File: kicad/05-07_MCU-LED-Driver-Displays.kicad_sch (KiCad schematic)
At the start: 57 parts, among them J4 Conn_01x03_Pin, J5 Conn_01x03_Pin, J7 Conn_02x05_Counter_Clockwise, Q4 AO3400A, Q5 AO3400A, SW1 USER_A, SW2 USER_B_PWR, SW3 RESET, SW4 BOOTSEL, U5 W25Q128JVS, U6 RP2040, Y1 ABM8-272-T3, Y2 ABS06-32.768-9-T

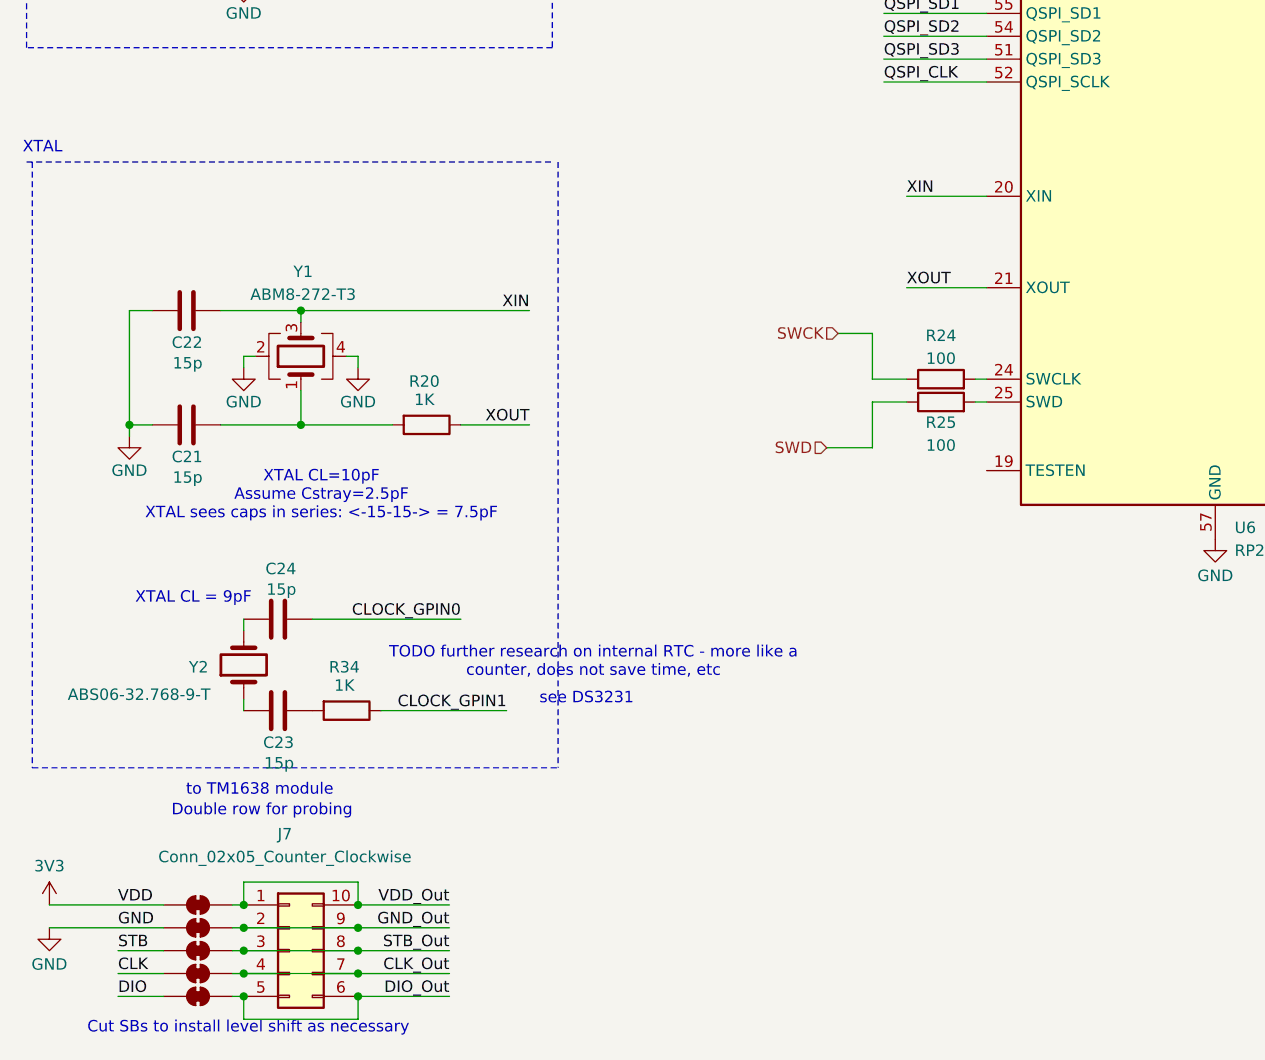
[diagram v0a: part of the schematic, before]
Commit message: external RTC start
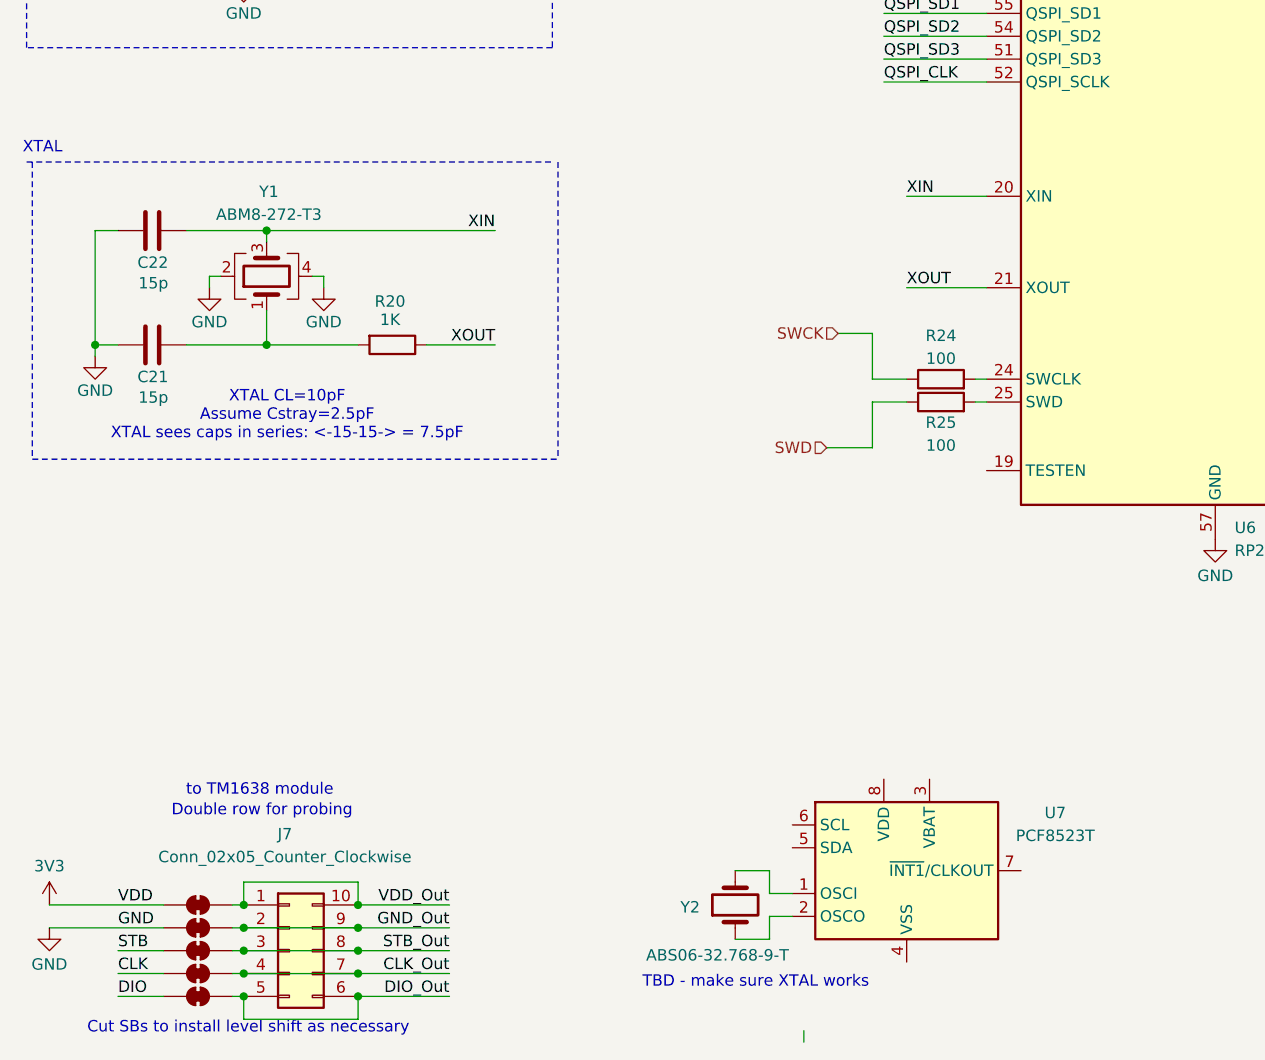
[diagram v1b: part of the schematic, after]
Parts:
- removed C23, C24: 15p, symbol Device:C
- removed R34: 1K, symbol Device:R
- added U7: PCF8523T, Package_SO:SOIC-8_3.9x4.9mm_P1.27mm, symbol Timer_RTC:PCF8523T
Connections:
- net at Y2.2: now also U7.1 (OSCI)
- net at Y2.1: now also U7.2 (OSCO)
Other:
- note added: "TBD - make sure XTAL works"
- note removed: "TODO further research on internal RTC - more like a counter, does not save time, etc"
- note removed: "XTAL CL = 9pF"
- note removed: "see DS3231"
- moved on the sheet: C21, C22, R20, Y1, Y2

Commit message: rtc research
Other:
- note added: "Can only use either INT1 or CLOCKOUT - not both"
- note added: "INT needs pullup Use INT1 for wakeup during dormant (active low) No need for Clock Out for RP2040 RTC"
- note added: "The most low power would be zero power alarm state on batt backup (DCDC off) - use INT1 to enable DCDC"
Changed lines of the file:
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@@
+		)
+	)
+	(text "Can only use either INT1 or CLOCKOUT - not both"
+		(exclude_from_sim no)
+		(at 137.668 189.484 0)
+		(effects
+			(font
+				(size 1.27 1.27)
+			)
 		)
 	)
@@
 		(exclude_from_sim no)
 		(at 49.53 23.876 0)
+		(effects
+			(font
+				(size 1.27 1.27)
+			)
+		)
+	)
+	(text "INT needs pullup\nUse INT1 for wakeup during dormant (active low)\nNo need for Clock Out for RP2040 RTC"
+		(exclude_from_sim no)
+		(at 151.13 181.864 0)
 		(effects
 			(font
@@
 		(effects
 			(font
+				(size 1.27 1.27)
+			)
+		)
+	)
+	(text "The most low power would be zero power alarm state\non batt backup (DCDC off)\n- use INT1 to enable DCDC "
+		(exclude_from_sim no)
+		(at 118.364 198.628 0)
+		(effects
+			(font

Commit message: rtc hardware
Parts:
- added C23, C24: 100n, symbol Device:C
- added J6: Conn_01x02_Pin, symbol Connector:Conn_01x02_Pin
- added JP10: SolderJumper_2_Open, symbol Jumper:SolderJumper_2_Open
- added R34, R35: 10K, symbol Device:R
- added R36: 1M, symbol Device:R
- Y2: value ABS06-32.768-9-T -> ABS07AIG-32.768KHZ-7-T; MPN (none) -> ABS07AIG-32.768KHZ-7-T; Manufacturer (none) -> Abracon LLC; Package (none) -> 2-SMD（3.2x1.5）; Supplier 1 (none) -> Digikey; Supplier 1 SKU (none) -> 535-13350-1-ND; Supplier 1 URL (none) -> https://www.digikey.jp/ja/products/detail/abracon-llc/ABS07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
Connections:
- net 3V3: now also U7.8 (VDD), C23.1, R34.2, R35.2, R36.2
- net GND: now also U7.4 (VSS), C23.2, C24.2, J6.2 (Pin_2)
- net Vbatt: now reaches U7.3 (VBAT)
- net Vbatt: now also C24.1
- net I2C_SDA: now reaches U7.5 (SDA)
- net I2C_SDA: now also R35.1
- net I2C_SCL: now reaches U7.6 (SCL)
- net I2C_SCL: now also R34.1
- net CLKOUT: now reaches U7.7 (~{INT1}/CLKOUT)
- net CLKOUT: now also J6.1 (Pin_1), JP10.1 (A)
- net ADC0_VBUS_In renamed ADC0_VUSB_In
- net CLOCK_GPIN0 renamed RTC_INT_GPIN0
- net RTC_INT_GPIN0: now also JP10.2 (B), R36.1
- net CLOCK_GPIN1: no longer names the net of U6.34 (GPIO22)
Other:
- note added: "LAYOUT: JP10 close to Pin"
- note added: "Probe CLKOut with 10:1 probe with JP10 = Open"
- note added: "RTC"
- note added: "Use XTAL with CL 7pF No need to add parasitics"
- note removed: "Can only use either INT1 or CLOCKOUT - not both"
- note removed: "INT needs pullup Use INT1 for wakeup during dormant (active low) No need for Clock Out for RP2040 RTC"
- note removed: "TBD - make sure XTAL works"
- note removed: "The most low power would be zero power alarm state on batt backup (DCDC off) - use INT1 to enable DCDC"
- moved on the sheet: C21, C22, R20, U7, Y1, Y2

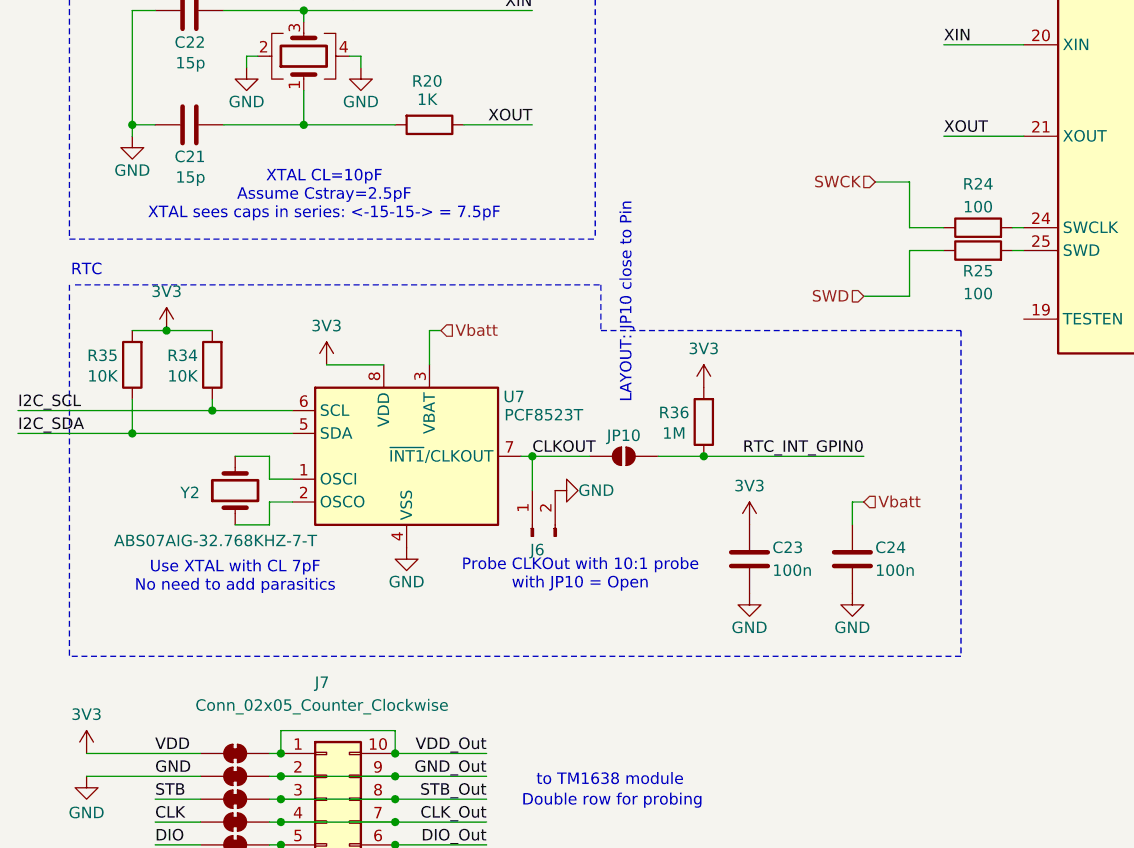
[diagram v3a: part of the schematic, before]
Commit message: rtc additions
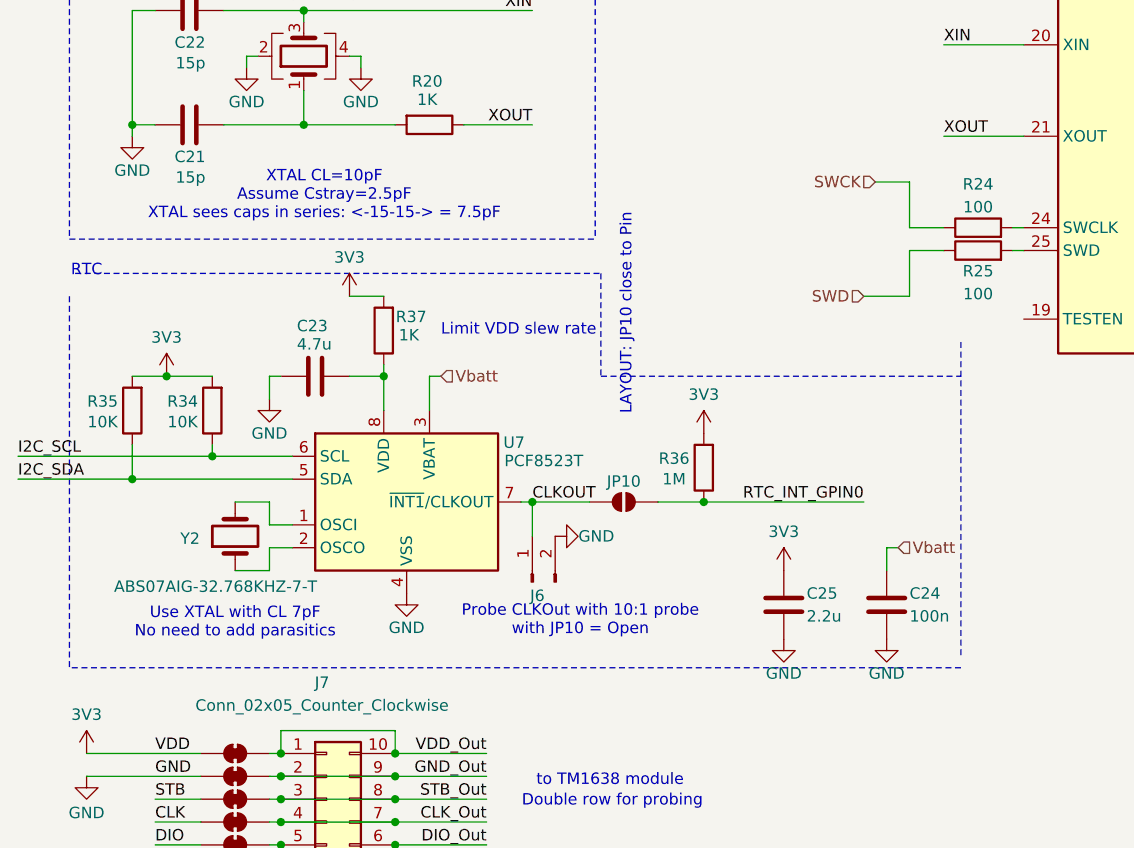
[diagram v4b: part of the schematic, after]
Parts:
- added C25: 2.2u, symbol Device:C
- added R37: 1K, symbol Device:R
- C23: value 100n -> 4.7u
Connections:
- net 3V3: now also C25.1, R37.2; no longer C23.1, U7.8 (VDD)
- net GND: now also C25.2
- new net: C23.1, R37.1, U7.8 (VDD)
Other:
- note added: "Limit VDD slew rate"
- moved on the sheet: C23, C24, J6, JP10, R34, R35, R36, U7, Y2

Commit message: buzzer
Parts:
- added BZ1: PKMCS0909E4000, symbol Device:Buzzer
- added R38: 1K, symbol Device:R
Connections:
- net Buzz_N: now reaches U6.11 (GPIO8)
- net Buzz_N: now also BZ1.2 (-)
- net Buzz_P: now reaches U6.9 (GPIO7)
- net Buzz_P: now also R38.2
- new net: BZ1.1 (+), R38.1
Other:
- note added: "Drive with Opposite Phase Square Wave, 4kHz"
